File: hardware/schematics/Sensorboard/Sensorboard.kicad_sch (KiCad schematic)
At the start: 79 parts, among them J1 Grauwasser, J3 BME680 #0 Innen, J4 RS485, J5 BME680 #1 Außen, J6 HX711 GasWaage, J7 LT452 Malibu, J8 Frischwasser, Q1 BSS138, Q2 BSS138, Q3 BSS138, Q4 AO3401A, Q5 2N7002, Q6 BSS138, Q7 BSS138, U1 ESP32-S3-DevKitC, U2 TSR2-2450, U3 LDL1117S33R, U4 SP3485CP, U5 PCF8523T, U6 BNO055, Y1 32.768

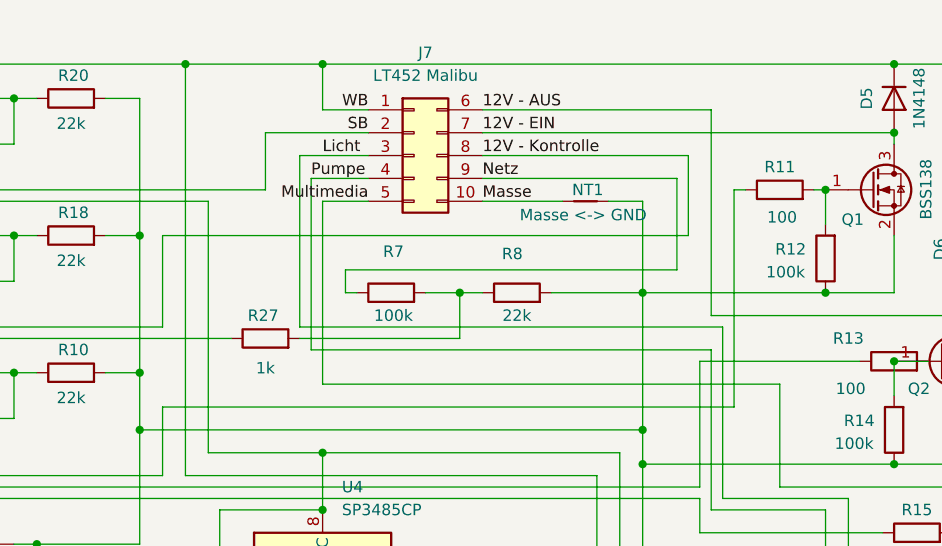
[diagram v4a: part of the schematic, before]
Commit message: feat/fix: BSEC 3.3V-Config, I2C-Recovery, Batt-Kali; Display + Hardware aktualisiert
Sensorboard:
- I2C Bus-Recovery (9 SCL-Pulse) für hängende Slaves (SDA klemmt LOW)
- BSEC 3.3V Pflicht-Konfiguration (bsec_config_33v_3s_4d) + HeatSource-Input
  (Standard-BSEC nutzt 1.8V – ohne Config sind IAQ-Werte dauerhaft falsch)
- Batterie-Kalibrierungsoffset 200 mV (BATT1 + BATT2)
- BME680 Board-Temperaturoffset 4.0 °C (SENSOR_BME680_TEMP_OFFSET_C)
- IAQ Accuracy-basiertes sofortiges State-Speichern (Bosch-Empfehlung)
- Dashboard HTML: Cache-Control no-store für HTML-Seiten; aktualisiertes dashboard.html

Display: Fonts (material_24 neu), rs485, main.c, display_config aktualisiert;
         LVGL-Docs + Demos entfernt (nicht benötigt)
Hardware: Sensorboard KiCad (PCB + Schaltplan) aktualisiert; SensorBee-Ordner neu
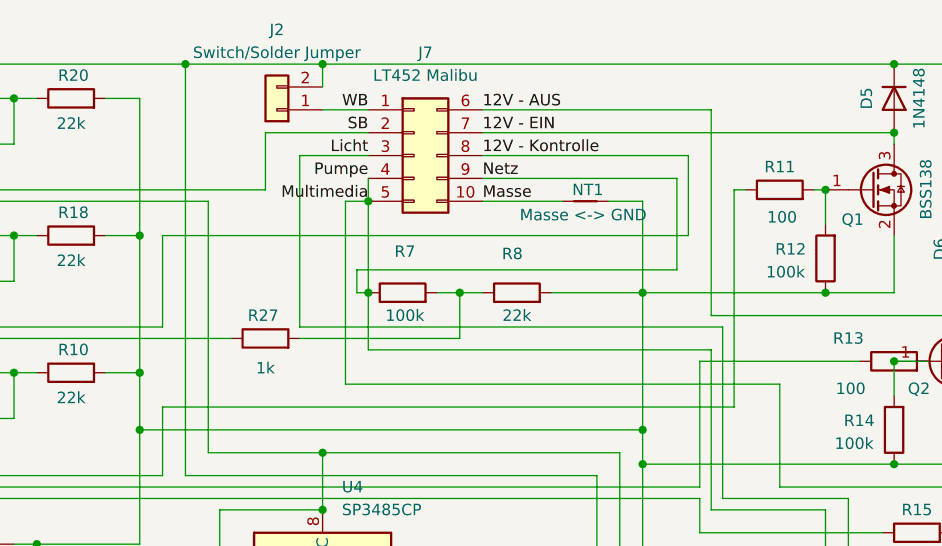
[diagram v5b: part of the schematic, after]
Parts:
- added J2: Switch/Solder Jumper, Connector_PinHeader_2.54mm:PinHeader_1x02_P2.54mm_Vertical, symbol Connector_Generic:Conn_01x02
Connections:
- net Netz is gone; now on net Multimedia: J7.9 (Pin_9), R7.1
- net Pumpe is gone; now on net Multimedia: D4.2 (A), J7.4 (Pin_4), Q6.3 (D)
- net WB: now also J2.1 (Pin_1); no longer C1.1, D3.1 (K), D4.1 (K), D5.1 (K), D6.1 (K), D7.1 (K), J1.1 (Pin_1), J8.1 (Pin_1), R19.1, U2.1 (Vin)
- new net: C1.1, D3.1 (K), D4.1 (K), D5.1 (K), D6.1 (K), D7.1 (K), J1.1 (Pin_1), J2.2 (Pin_2), J8.1 (Pin_1), R19.1, U2.1 (Vin)
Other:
- moved on the sheet: R7
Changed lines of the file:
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@@
 	)
 	(junction
+		(at 194.31 17.78)
+		(diameter 0)
+		(color 0 0 0 0)
+	)
+	(junction
 		(at 33.02 99.06)
 		(diameter 0)
@@
 	)
 	(junction
+		(at 199.39 43.18)
+		(diameter 0)
+		(color 0 0 0 0)
+	)
+	(junction
 		(at 82.55 48.26)
 		(diameter 0)
@@
 	)
 	(junction
+		(at 199.39 33.02)
+		(diameter 0)
+		(color 0 0 0 0)
+	)
+	(junction
 		(at 270.51 97.79)
 		(diameter 0)
@@
 	)
 	(junction
-		(at 194.31 17.78)
-		(diameter 0)
-		(color 0 0 0 0)
-	)
-	(junction
 		(at 31.75 53.34)
 		(diameter 0)
@@
 	(wire
 		(pts
-			(xy 194.31 53.34) (xy 194.31 33.02)
+			(xy 196.85 53.34) (xy 196.85 33.02)
 		)
 		(stroke
@@
 	(wire
 		(pts
+			(xy 199.39 43.18) (xy 199.39 33.02)
+		)
+		(stroke
+			(width 0)
+			(type default)
+		)
+	)
+	(wire
+		(pts
 			(xy 278.13 17.78) (xy 273.05 17.78)
 		)
@@
 	(wire
 		(pts
-			(xy 205.74 43.18) (xy 209.55 43.18)
+			(xy 207.01 43.18) (xy 209.55 43.18)
 		)
 		(stroke
@@
 	(wire
 		(pts
-			(xy 194.31 22.86) (xy 199.39 22.86)
-		)
-		(stroke
-			(width 0)
-			(type default)
-		)
-	)
-	(wire
-		(pts
 			(xy 44.45 40.64) (xy 44.45 48.26)
 		)
@@
 	(wire
 		(pts
-			(xy 194.31 17.78) (xy 194.31 22.86)
-		)
-		(stroke
-			(width 0)
-			(type default)
-		)
-	)
-	(wire
-		(pts
 			(xy 160.02 21.59) (xy 162.56 21.59)
 		)
@@
 	(wire
 		(pts
-			(xy 237.49 49.53) (xy 193.04 49.53)
+			(xy 237.49 49.53) (xy 199.39 49.53)
 		)
 		(stroke
@@
 	(wire
 		(pts
-			(xy 196.85 43.18) (xy 198.12 43.18)
+			(xy 198.12 43.18) (xy 199.39 43.18)
 		)
 		(stroke
@@
 	(wire
 		(pts
-			(xy 196.85 40.64) (xy 196.85 43.18)
+			(xy 198.12 40.64) (xy 198.12 43.18)
 		)
 		(stroke
@@
 	(wire
 		(pts
-			(xy 245.11 53.34) (xy 194.31 53.34)
+			(xy 245.11 53.34) (xy 196.85 53.34)
 		)
 		(stroke
@@
 	(wire
 		(pts
-			(xy 193.04 49.53) (xy 193.04 30.48)
+			(xy 199.39 49.53) (xy 199.39 43.18)
 		)
 		(stroke
@@
 	(wire
 		(pts
+			(xy 194.31 17.78) (xy 257.81 17.78)
+		)
+		(stroke
+			(width 0)
+			(type default)
+		)
+	)
+	(wire
+		(pts
 			(xy 128.27 138.43) (xy 125.73 138.43)
 		)
@@
 	(wire
 		(pts
+			(xy 194.31 17.78) (xy 194.31 20.32)
+		)
+		(stroke
+			(width 0)
+			(type default)
+		)
+	)
+	(wire
+		(pts
 			(xy 186.69 115.57) (xy 189.23 115.57)
 		)
@@
 	(wire
 		(pts
-			(xy 196.85 40.64) (xy 233.68 40.64)
+			(xy 198.12 40.64) (xy 233.68 40.64)
 		)
 		(stroke
@@
 	(wire
 		(pts
-			(xy 193.04 30.48) (xy 199.39 30.48)
-		)
-		(stroke
-			(width 0)
-			(type default)
-		)
-	)
-	(wire
-		(pts
 			(xy 176.53 46.99) (xy 176.53 36.83)
 		)
@@
 	(wire
 		(pts
-			(xy 194.31 33.02) (xy 199.39 33.02)
+			(xy 196.85 33.02) (xy 199.39 33.02)
 		)
 		(stroke
@@
 	(wire
 		(pts
-			(xy 194.31 17.78) (xy 257.81 17.78)
-		)
-		(stroke
-			(width 0)
-			(type default)
-		)
-	)
-	(wire
-		(pts
 			(xy 135.89 83.82) (xy 135.89 118.11)
 		)
@@
 	(wire
 		(pts
+			(xy 194.31 22.86) (xy 199.39 22.86)
+		)
+		(stroke
+			(width 0)
+			(type default)
+		)
+	)
+	(wire
+		(pts
 			(xy 182.88 101.6) (xy 194.31 101.6)
 		)
@@
 	(wire
 		(pts
+			(xy 199.39 33.02) (xy 199.39 30.48)
+		)
+		(stroke
+			(width 0)
+			(type default)
+		)
+	)
+	(wire
+		(pts
 			(xy 229.87 43.18) (xy 250.19 43.18)
 		)
@@
 	)
 	(label "Pumpe"
-		(at 193.04 30.48 0)
+		(at 199.39 30.48 180)
 		(effects
 			(font
 				(size 1.27 1.27)
 			)
-			(justify left bottom)
+			(justify right bottom)
 		)
 	)
@@
 	)
 	(label "Licht"
-		(at 194.31 27.94 0)
+		(at 199.39 27.94 180)
 		(effects
 			(font
 				(size 1.27 1.27)
 			)
-			(justify left bottom)
+			(justify right bottom)
 		)
 	)
@@
 	(symbol
 		(lib_id "Device:R")
-		(at 201.93 43.18 90)
+		(at 203.2 43.18 90)
 		(unit 1)
 		(exclude_from_sim no)
@@
 		(dnp no)
 		(property "Reference" "R7"
-			(at 202.184 38.608 90)
+			(at 203.454 38.608 90)
 			(effects
 				(font
@@
 		)
 		(property "Value" "100k"
-			(at 202.184 45.72 90)
+			(at 203.454 45.72 90)
 			(effects
 				(font
@@
 		)
 		(property "Footprint" "Resistor_SMD:R_0402_1005Metric"
-			(at 201.93 44.958 90)
+			(at 203.2 44.958 90)
 			(effects
 				(font
@@
 		)
 		(property "Datasheet" "~"
-			(at 201.93 43.18 0)
+			(at 203.2 43.18 0)
 			(effects
 				(font
@@
 		)
 		(property "Description" "Resistor 0805 Thin-Film, 0.1%, 25–50 ppm Susumu"
-			(at 201.93 43.18 0)
+			(at 203.2 43.18 0)
 			(effects
 				(font
@@
 					(unit 1)
 				)
+			)
+		)
+	)
+	(symbol
+		(lib_id "Connector_Generic:Conn_01x02")
+		(at 189.23 22.86 180)
+		(unit 1)
+		(exclude_from_sim no)
+		(in_bom yes)
+		(on_board yes)
+		(dnp no)
+		(fields_autoplaced yes)
+		(property "Reference" "J2"
+			(at 189.23 13.97 0)
+			(effects
+				(font
+					(size 1.27 1.27)
+				)
+			)
+		)
+		(property "Value" "Switch/Solder Jumper"
+			(at 189.23 16.51 0)
+			(effects
+				(font
+					(size 1.27 1.27)
+				)
+			)
+		)
+		(property "Footprint" "Connector_PinHeader_2.54mm:PinHeader_1x02_P2.54mm_Vertical"
+			(at 189.23 22.86 0)
+			(effects
+				(font
+					(size 1.27 1.27)
+				)
+				(hide yes)
+			)
+		)
+		(property "Datasheet" "~"
+			(at 189.23 22.86 0)
+			(effects
+				(font
+					(size 1.27 1.27)
+				)
+				(hide yes)
+			)
+		)
+		(property "Description" "Generic connector, single row, 01x02, script generated (kicad-library-utils/schlib/autogen/connector/)"
+			(at 189.23 22.86 0)
+			(effects
+				(font
+					(size 1.27 1.27)
+				)
+				(hide yes)
+			)
+		)
+		(pin "2"
+		)
+		(pin "1"
+		)
+		(instances
+			(project ""
+				(path "/b669c17f-1210-4a4a-a19b-da2f4a50bcdd"
+					(reference "J2")
+					(unit 1)
+				)
